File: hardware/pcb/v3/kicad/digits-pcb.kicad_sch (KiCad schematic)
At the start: 44 parts, among them J8 Conn_01x04, SW1 Hook_DPDT, SW2 SW_Push, U3 RP2040, U4 W25Q16JVSSIQ, U5 AMS1117-3.3, Y1 ABM8-272-T3

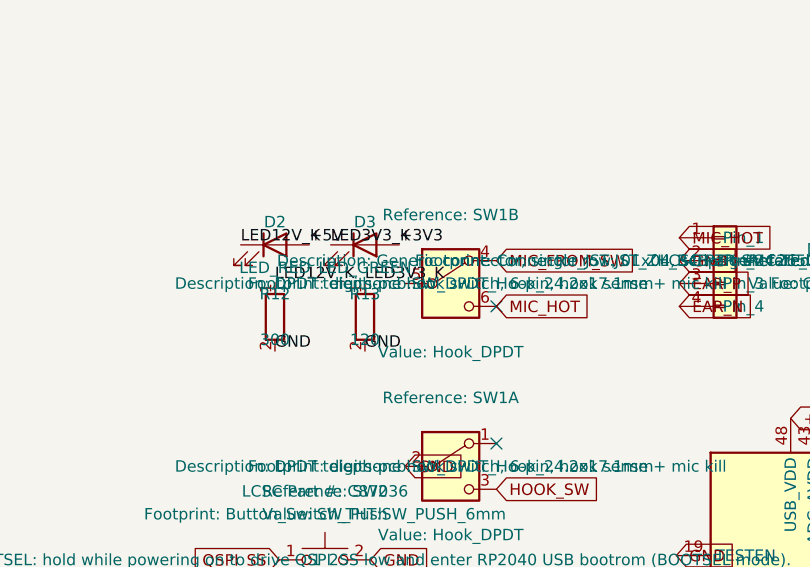
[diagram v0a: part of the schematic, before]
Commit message: fix(hardware): correct V3 PCB Y-mirrored footprints, restore nets, add thermal vias
All IC footprints in V3 had Y-mirrored pad coordinates from an early
front/back flip during board creation. Every IC would have had pins
connected to wrong nets. Updated all footprints from the KiCad library
to restore correct pad geometry.

Additional fixes:
- Restored net assignments on PI_ZERO_W1 (40-pin Pi header) and U6
  (TLV320AIC3104 codec) that were lost during footprint repair
- Added GND thermal vias under U3 (RP2040, 3x3), U6 (TLV320AIC3104,
  3x3), and U2 (DRV8871, 2x2) exposed pads
- Fixed layer stackup metadata: F.SilkS/B.SilkS/F.CrtYd/B.CrtYd user
  names were swapped from the original flip operation
- Removed dangling MIC_FROM_SW via and XOUT_MCU track stubs
- Added no-connect flag on SW1 pin 5 (unused pole B throw)
- Fixed R13 LCSC part number in COMPONENTS.md (C25752 to C25079)
- Updated NET_TOPOLOGY.md mounting hole coordinates to actual V3
  positions (were stale V2 values since initial creation)
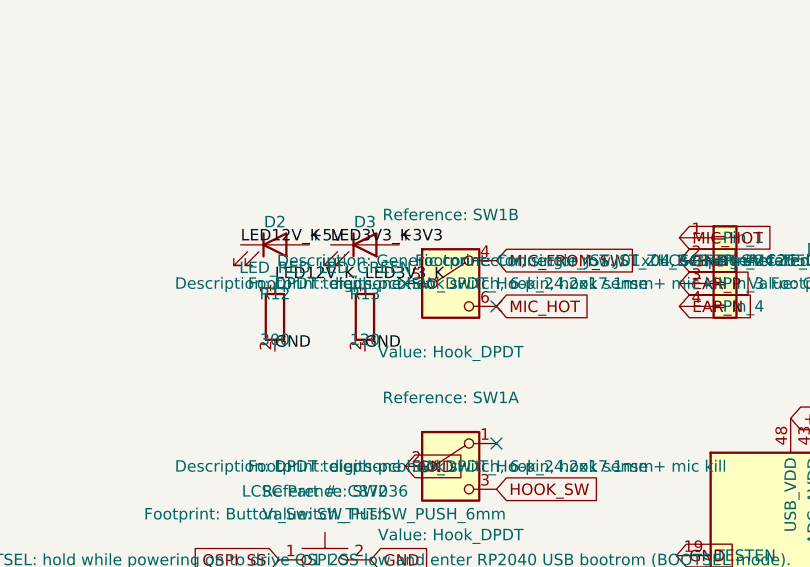
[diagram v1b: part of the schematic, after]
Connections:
- no-connect marks 39 -> 40
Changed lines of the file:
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@@
 		(at 175.26 101.6)
+	)
+	(no_connect
+		(at 44.45 34.29)
 	)
 	(wire
